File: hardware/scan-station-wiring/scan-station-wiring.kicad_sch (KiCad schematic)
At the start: 76 parts, among them J10 Buttons/Encoder, J12 USB-C Host, J13 RJ45 MagJack, J14 PoE Module Input, J15 PoE Module Output (5V), J16 Load Cell 2, J1A CYD Expansion (SPI2), J1B CYD UART (PWR+HS), J2 NFC Antenna A, J3 RGB LED Header, J4 NFC Antenna B, J5 USB-C, J6 Load Cell, J7 CAN Bus, J8 I2C1 Expansion, J9 TOF Sensor (I2C1), Q1 TVDD_SW_A, Q2 P-MOS TVDD_SW_B, Q3 BSS138 (SDA), Q4 BSS138 (SCL), SW1 RESET, SW2 BOOT, U1 ESP32-S3-WROOM-1-N16R8, U10 W5500, U2 ADS1220IPWR, U3 AHT20, U4 PN5180A0HN, U5 AS7341-DLGM, U6 AMS1117-3.3, U7 SN65HVD230DR, U8 AMS1117-1.8, U9 CH340C, Y1 27.12MHz

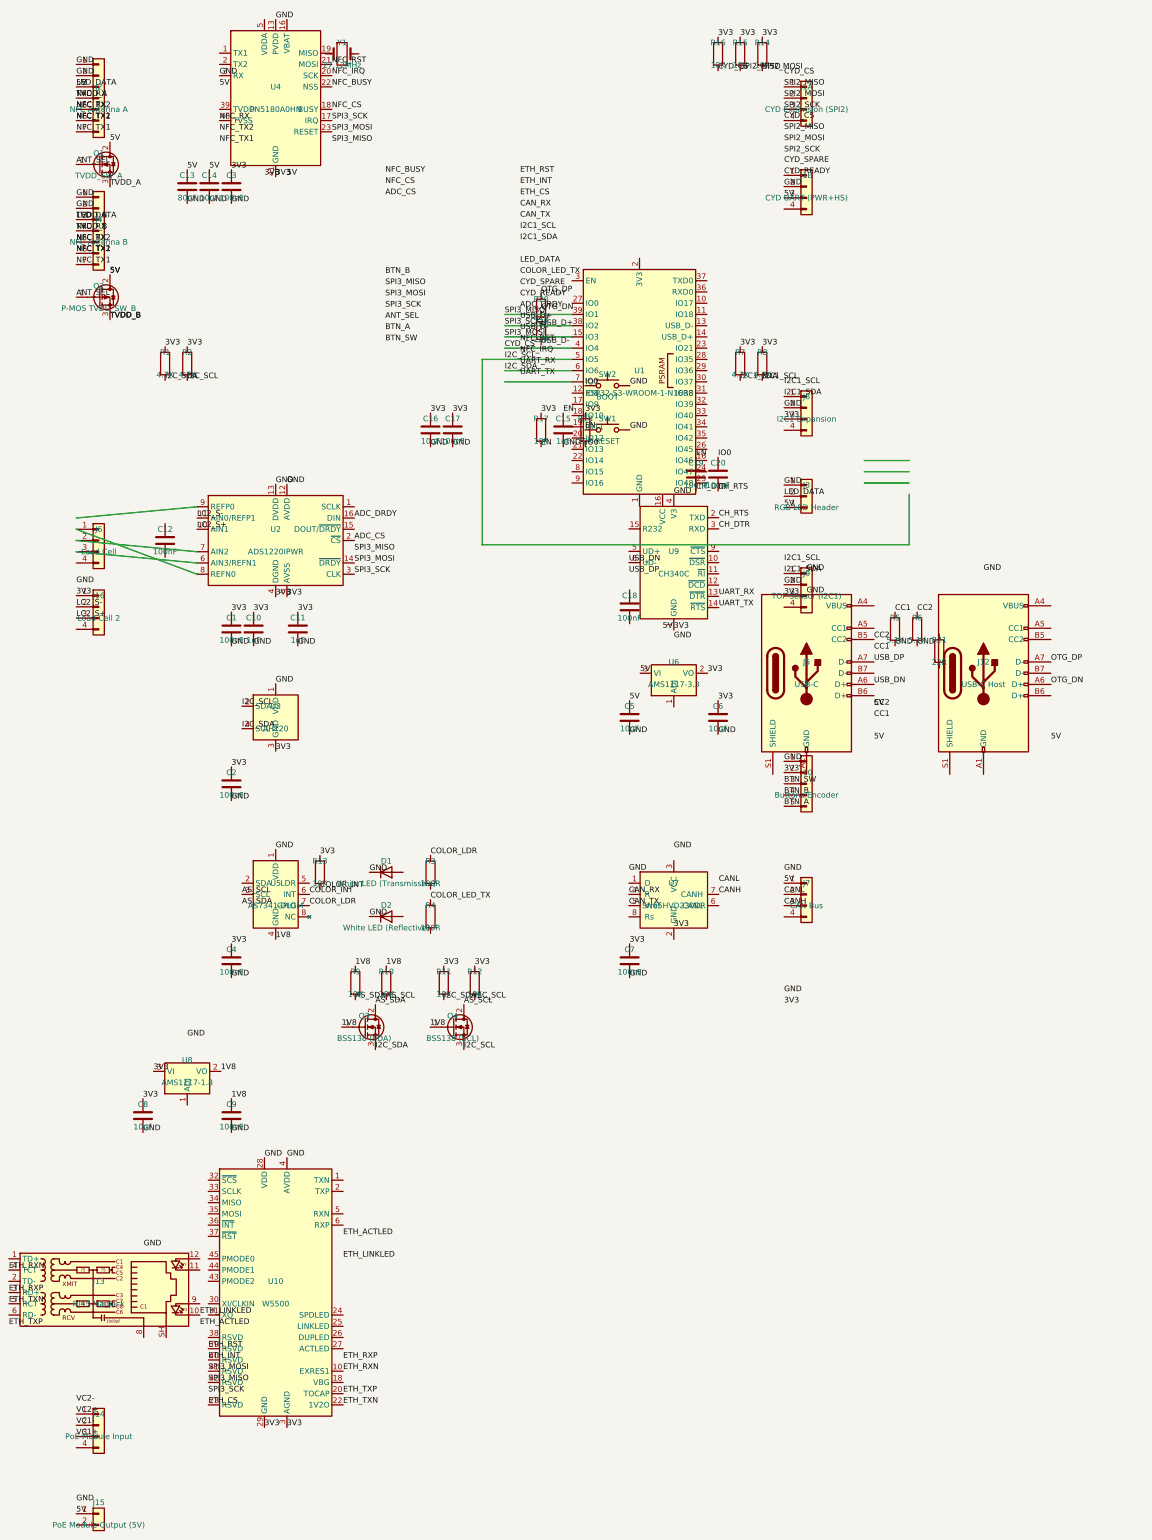
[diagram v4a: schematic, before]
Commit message: feat: upgrade connectors and fix USB routing
- Swap RJ45 MagJack to JK00177 with PoE center-taps and LEDs
  VC1+/VC1-/VC2+/VC2- wired to J14 PoE module header
  LED1 → ETH_LINKLED, LED2 → ETH_ACTLED (from W5500)
- Upgrade both USB-C to 16P receptacles (full pin redundancy)
- Fix USB data routing:
  J5 (programming): CH_DN/CH_DP → CH340C (isolated from ESP32)
  J12 (host): OTG_DN/OTG_DP → series resistors → ESP32 IO19/IO20
- Add HOST_CC1/CC2 pull-up resistors (R22/R23, 5.1K to 5V)
  for USB-C host mode advertisement on J12
- ERC passes clean

Co-Authored-By: Claude Opus 4.6 (1M context) <noreply@anthropic.com>
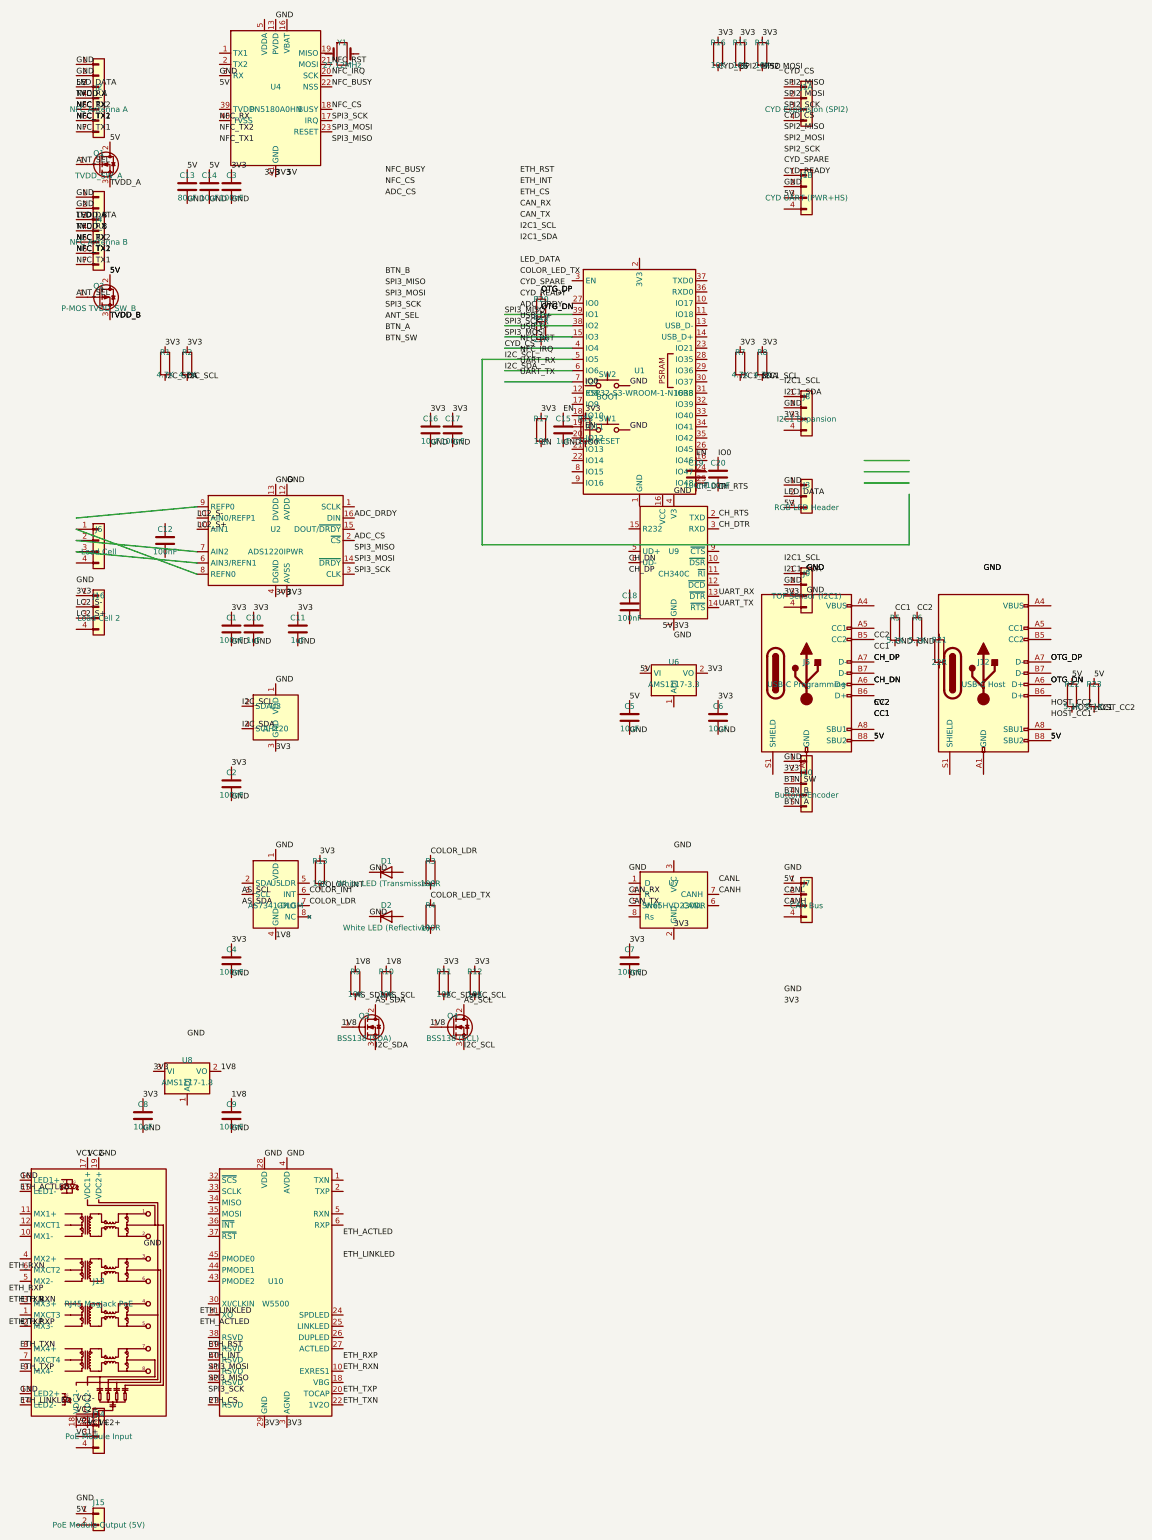
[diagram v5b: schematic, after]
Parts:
- removed J12: USB-C Host, symbol Connector:USB_C_Receptacle_USB2.0_14P
- removed J13: RJ45 MagJack, symbol Connector:RJ45_Hanrun_HR911105A_Horizontal
- removed J5: USB-C, symbol Connector:USB_C_Receptacle_USB2.0_14P
- added J12: USB-C Host, symbol Connector:USB_C_Receptacle_USB2.0_16P
- added J13: RJ45 MagJack PoE, symbol Connector:RJ45_JK00177
- added J5: USB-C Programming, symbol Connector:USB_C_Receptacle_USB2.0_16P
- added R22, R23: 5.1K, symbol Device:R
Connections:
- net 5V: now also J12.B8 (SBU2), J5.B5 (CC2), J5.B8 (SBU2), R22.1, R23.1
- net ETH_ACTLED: now also J13.15 (LED1-)
- net ETH_LINKLED: now also J13.14 (LED2-)
- net ETH_RXN: now also J13.3 (MX3+)
- net ETH_RXP: now also J13.2 (MX3-)
- net ETH_TXN: now also J13.8 (MX4+)
- net ETH_TXP: now also J13.9 (MX4-)
- net GND: now also J13.13 (LED2+), J13.16 (LED1+), J13.19 (VDC2+)
- net OTG_DN: now also J12.A6 (D+)
- net OTG_DP: now also J12.A7 (D-)
- net USB_D+: no longer R20.2
- net USB_D-: no longer R19.2
- net VC1+: now also J13.20 (VDC2-)
- net VC2+: now also J13.SH
- net VC2-: now also J13.17 (VDC1+)
- net USB_DN renamed CH_DN
- net CH_DN: now also J5.A6 (D+)
- new net: J5.A1 (GND), J5.A12 (GND), J5.B1 (GND), J5.B12 (GND)
- new net: J5.A4 (VBUS), J5.A9 (VBUS), J5.B4 (VBUS), J5.B9 (VBUS)
- new net: J12.A1 (GND), J12.A12 (GND), J12.B1 (GND), J12.B12 (GND)
- new net: J12.A4 (VBUS), J12.A9 (VBUS), J12.B4 (VBUS), J12.B9 (VBUS)
- new net CH_DP: J5.A7 (D-)
- new net HOST_CC1: R22.2
- new net HOST_CC2: R23.2

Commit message: chore: final label cleanup — remove 22 orphans, fix USB chain
- Remove 14 duplicate labels at same positions
- Remove 6 old HR911105A MagJack labels (replaced by JK00177)
- Add USB_D+/USB_D- labels on R19/R20 ESP32-side pins
  completing the chain: ESP32 → USB_D±  → R19/R20 → OTG_D± → J12
- Pretty-print schematic file
- All 74 nets have 2+ endpoints, zero single-endpoint orphans
- ERC: 0 errors, 0 warnings

Co-Authored-By: Claude Opus 4.6 (1M context) <noreply@anthropic.com>
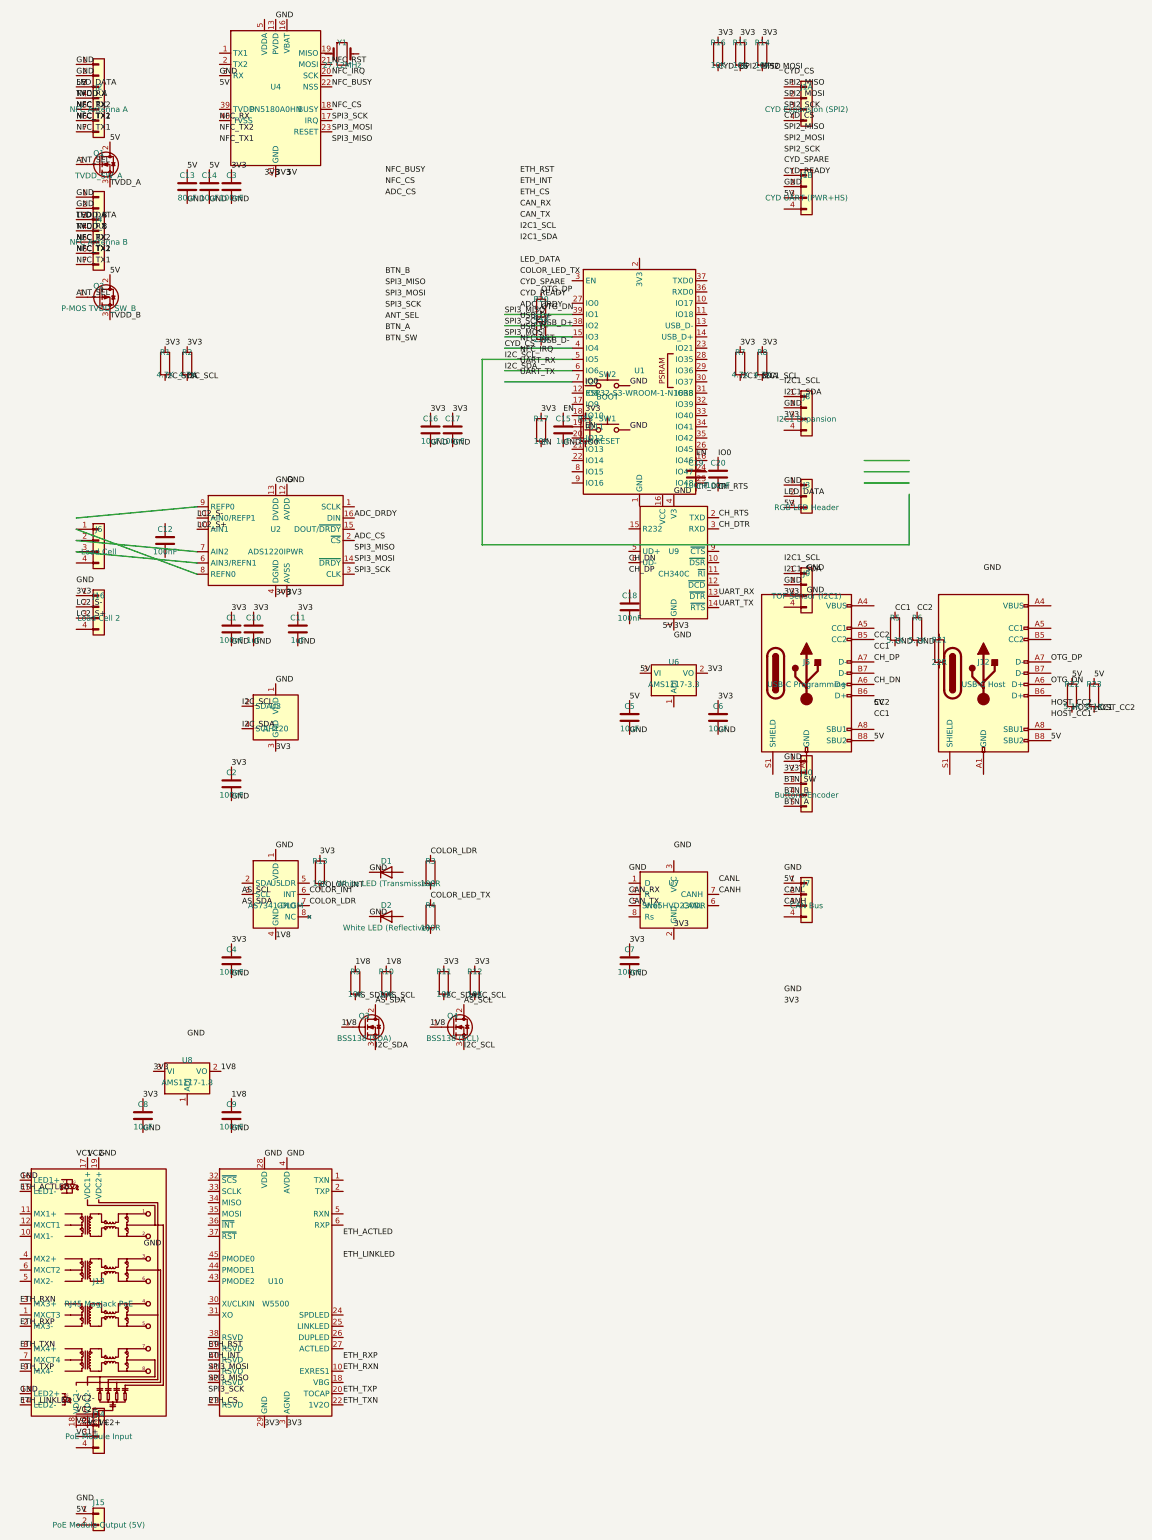
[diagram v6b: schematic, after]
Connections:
- net USB_D+: now also R20.2
- net USB_D-: now also R19.2

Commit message: feat: assign footprints to all 78 components
All components now have footprint assignments for PCB layout:
- ICs: WROOM-1, TSSOP-16, QFN-40, SOIC-8, SOT-223, SOP-16, LQFP-48
- Passives: 0603 (R, small C), 0805 (10uF), 1210 (80uF bulk)
- MOSFETs/BSS138: SOT-23
- LEDs: 0603
- Buttons: TL3342 SMD tactile
- Crystal: SMD 3215
- USB-C: HRO TYPE-C-31-M-12 (16P, high quality)
- RJ45: Amphenol RJMG1BD3B8K1ANR (PoE + LEDs)
- I2C/CYD: JST SH 1.00mm (Qwiic-compatible)
- General: 2.54mm pin headers

ERC: 0 errors, 0 warnings.

Co-Authored-By: Claude Opus 4.6 (1M context) <noreply@anthropic.com>
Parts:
- C1, C10, C11, C12, C15, C17, C18, C19, C2, C20, C3, C4, C7, C9: footprint (none) -> Capacitor_SMD:C_0603_1608Metric
- C13: footprint (none) -> Capacitor_SMD:C_1210_3225Metric
- C14, C16, C5, C6, C8: footprint (none) -> Capacitor_SMD:C_0805_2012Metric
- D1, D2: footprint (none) -> LED_SMD:LED_0603_1608Metric
- J10: footprint (none) -> Connector_PinHeader_2.54mm:PinHeader_1x05_P2.54mm_Vertical
- J12, J5: footprint (none) -> Connector_USB:USB_C_Receptacle_HRO_TYPE-C-31-M-12
- J13: footprint (none) -> Connector_RJ:RJ45_Amphenol_RJMG1BD3B8K1ANR
- J14, J16, J6, J7: footprint (none) -> Connector_PinHeader_2.54mm:PinHeader_1x04_P2.54mm_Vertical
- J15: footprint (none) -> Connector_PinHeader_2.54mm:PinHeader_1x02_P2.54mm_Vertical
- J1A, J1B, J8, J9: footprint (none) -> Connector_JST:JST_SH_SM04B-SRSS-TB_1x04-1MP_P1.00mm_Horizontal
- J2, J4: footprint (none) -> Connector_PinHeader_2.54mm:PinHeader_1x07_P2.54mm_Vertical
- J3: footprint (none) -> Connector_PinHeader_2.54mm:PinHeader_1x03_P2.54mm_Vertical
- Q1, Q2, Q3, Q4: footprint (none) -> Package_TO_SOT_SMD:SOT-23
- R1, R10, R11, R12, R13, R14, R15, R16, R17, R18, R19, R2, R20, R21, R22, R23, R3, R4, R5, R6, R7, R8, R9: footprint (none) -> Resistor_SMD:R_0603_1608Metric
- SW1, SW2: footprint (none) -> Button_Switch_SMD:SW_SPST_TL3342
- U1: footprint (none) -> RF_Module:ESP32-S3-WROOM-1
- U10: footprint (none) -> Package_QFP:LQFP-48_7x7mm_P0.5mm
- U2: footprint (none) -> Package_SO:TSSOP-16_4.4x5mm_P0.65mm
- U3: footprint (none) -> Package_DFN_QFN:DFN-4-1EP_2x2mm_P0.65mm
- U4: footprint (none) -> Package_DFN_QFN:QFN-40-1EP_6x6mm_P0.5mm
- U5: footprint (none) -> Package_DFN_QFN:DFN-8-1EP_3x2mm_P0.5mm
- U6, U8: footprint (none) -> Package_TO_SOT_SMD:SOT-223-3_TabPin2
- U7: footprint (none) -> Package_SO:SOIC-8_3.9x4.9mm_P1.27mm
- U9: footprint (none) -> Package_SO:SOP-16_3.9x9.9mm_P1.27mm
- Y1: footprint (none) -> Crystal:Crystal_SMD_3215-2Pin_3.2x1.5mm

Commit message: fix: correct footprint assignments for ICs
- U3 (AHT20): Aosong_AHT20 (was wrong QFN-40)
- U4 (PN5180): HVQFN-40-1EP_6x6mm with thermal vias
- U5 (AS7341): AMS_LGA-8_2x3.1mm (was wrong DFN-4)
- U6/U8 (AMS1117): SOT-223-3_TabPin2
- U9 (CH340C): SOIC-16 (was wrong SOP-16)

Co-Authored-By: Claude Opus 4.6 (1M context) <noreply@anthropic.com>
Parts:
- U3: footprint Package_DFN_QFN:DFN-4-1EP_2x2mm_P0.65mm -> Sensor:Aosong_AHT20
- U4: footprint Package_DFN_QFN:QFN-40-1EP_6x6mm_P0.5mm -> Package_DFN_QFN:HVQFN-40-1EP_6x6mm_P0.5mm_ThermalVias
- U5: footprint Package_DFN_QFN:DFN-8-1EP_3x2mm_P0.5mm -> Package_LGA:AMS_LGA-8_2x3.1mm_P0.8mm
- U9: footprint Package_SO:SOP-16_3.9x9.9mm_P1.27mm -> Package_SO:SOIC-16_3.9x9.9mm_P1.27mm
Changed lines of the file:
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@@
       (effects (font (size 1.27 1.27)))
     )
-    (property "Footprint" "Package_DFN_QFN:DFN-4-1EP_2x2mm_P0.65mm"
+    (property "Footprint" "Sensor:Aosong_AHT20"
       (at 60 180 0)
       (effects (font (size 1.27 1.27)) (hide yes))
@@
       (effects (font (size 1.27 1.27)))
     )
-    (property "Footprint" "Package_DFN_QFN:QFN-40-1EP_6x6mm_P0.5mm"
+    (property "Footprint" "Package_DFN_QFN:HVQFN-40-1EP_6x6mm_P0.5mm_ThermalVias"
       (at 60 40 0)
       (effects (font (size 1.27 1.27)) (hide yes))
@@
       (effects (font (size 1.27 1.27)))
     )
-    (property "Footprint" "Package_DFN_QFN:DFN-8-1EP_3x2mm_P0.5mm"
+    (property "Footprint" "Package_LGA:AMS_LGA-8_2x3.1mm_P0.8mm"
       (at 60 220 0)
       (effects (font (size 1.27 1.27)) (hide yes))
@@
       (effects (font (size 1.27 1.27)))
     )
-    (property "Footprint" "Package_SO:SOP-16_3.9x9.9mm_P1.27mm"
+    (property "Footprint" "Package_SO:SOIC-16_3.9x9.9mm_P1.27mm"
       (at 150 145 0)
       (effects (font (size 1.27 1.27)) (hide yes))
